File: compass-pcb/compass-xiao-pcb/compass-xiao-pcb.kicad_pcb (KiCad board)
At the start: 2 copper layers, 72.2 x 72 mm, 24 parts

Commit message: polishing
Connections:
- QMC5883L pad 3: (no net) -> GND
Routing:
- net (no net): track 1108.9 -> 1118.5 mm
- net GND: track 1.55 -> 8.21 mm
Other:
- board text removed: "VCC GND SCL SDA"

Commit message: fixing ground
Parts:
- REF**: value TX, RX, GND -> TX, RX
- REF**: value SCL,SDA,VCC -> VCC,SCL,SDA
- moved REF** 5.20 mm to (241.2, 47.3), turned to 90 degrees
- moved REF** 5.19 mm to (241.2, 51.6), turned to 90 degrees
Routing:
- net (no net): track 1118.5 -> 1129.4 mm
- net GND: track 8.21 -> 16.7 mm, vias 0 -> 1

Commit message: lots of pcb fixes
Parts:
- moved 49E Hall 168.5 mm to (74.5, 92.7)
- moved A1SHB 168.4 mm to (40.2, 84.6)
- moved QMC5883L 168.4 mm to (28.4, 78.7)
- moved USB / Charge 168.4 mm to (45.9, 65.4)
- moved 10K 168.4 mm to (35.0, 37.4)
- moved 10K 168.4 mm to (40.3, 80.9)
- moved 1N4148 168.4 mm to (39.1, 35.3)
- moved 51 168.4 mm to (40.2, 93.1)
- moved 51 168.4 mm to (40.3, 88.4)
- moved 51 168.4 mm to (40.2, 90.7)
- moved A1SHB 168.4 mm to (40.2, 31.3)
- moved Battery 168.4 mm to (71.4, 88.9)
- moved LEDs 168.4 mm to (30.0, 84.0)
- moved REF** 168.4 mm to (73.7, 27.2)
- moved REF** 168.4 mm to (26.0, 58.3)
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- renumbered 56 to 51
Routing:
- net GND: track 16.7 -> 23.1 mm
- net (no net): track 1129.4 -> 1134.9 mm
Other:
- outline, holes or cut-outs redrawn
- board text added: "3.7V 5V D- D+ GND"
- board text removed: "3.7V 5V D+ D- GND"

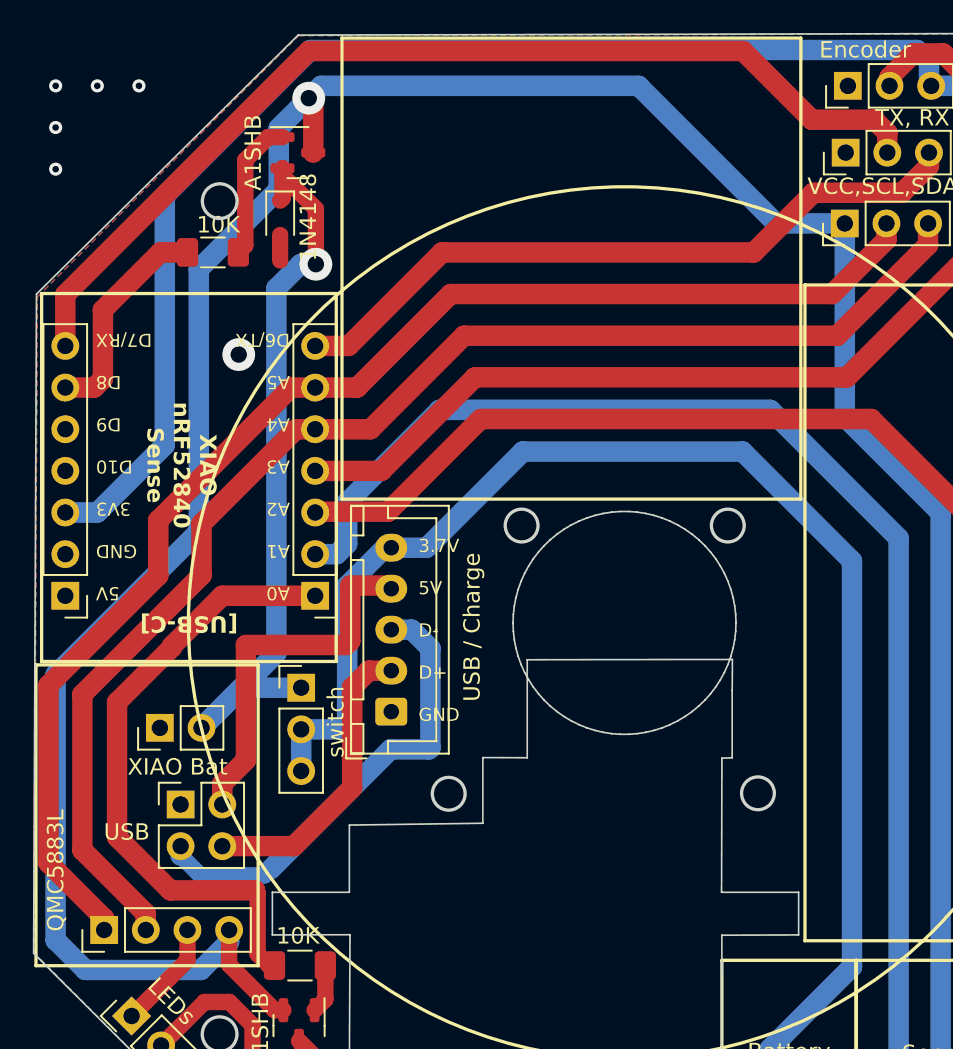
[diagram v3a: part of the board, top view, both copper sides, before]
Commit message: optimizing for cricut
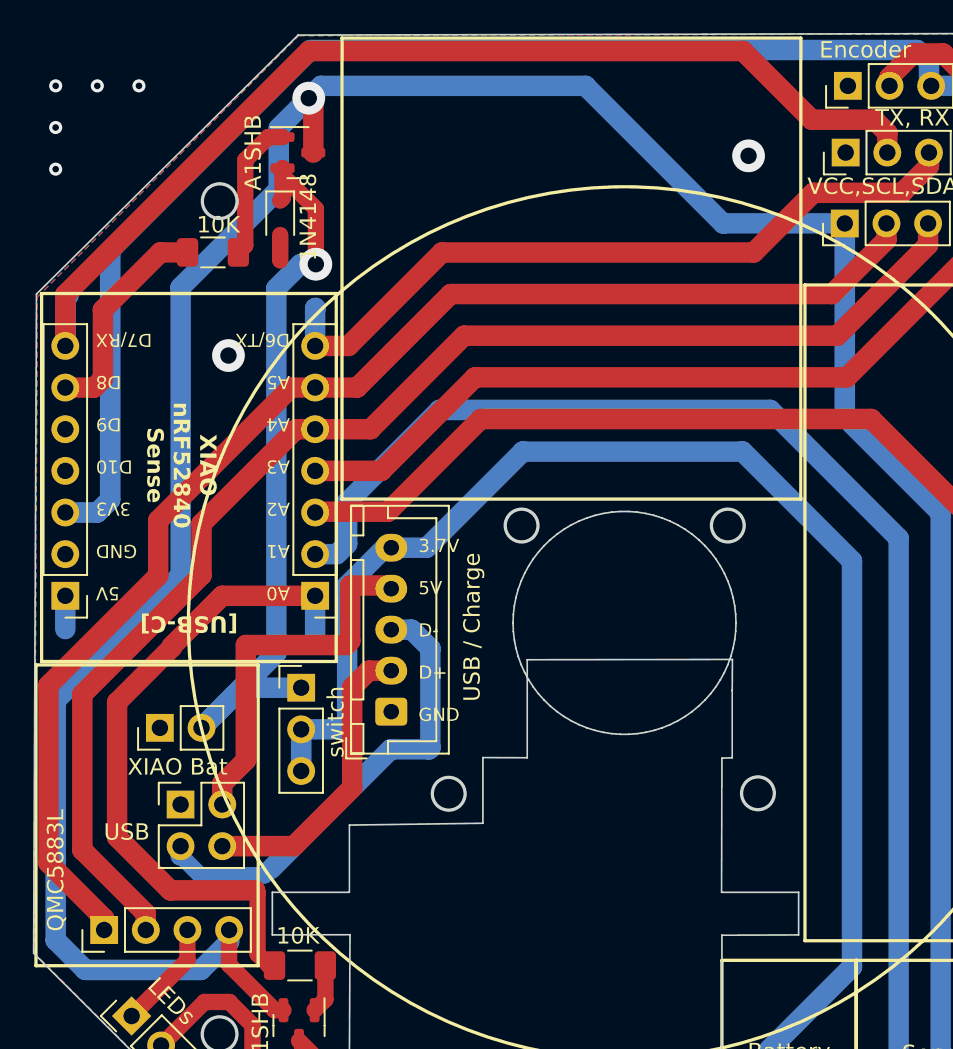
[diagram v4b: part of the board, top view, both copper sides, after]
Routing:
- net (no net): track 1134.9 -> 1145.3 mm
- net GND: vias 1 -> 2

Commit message: more polishing
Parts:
- moved 49E Hall 0.17 mm to (74.5, 92.5)
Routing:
- net (no net): track 1145.3 -> 1155.2 mm
- net GND: track 23.1 -> 31.4 mm

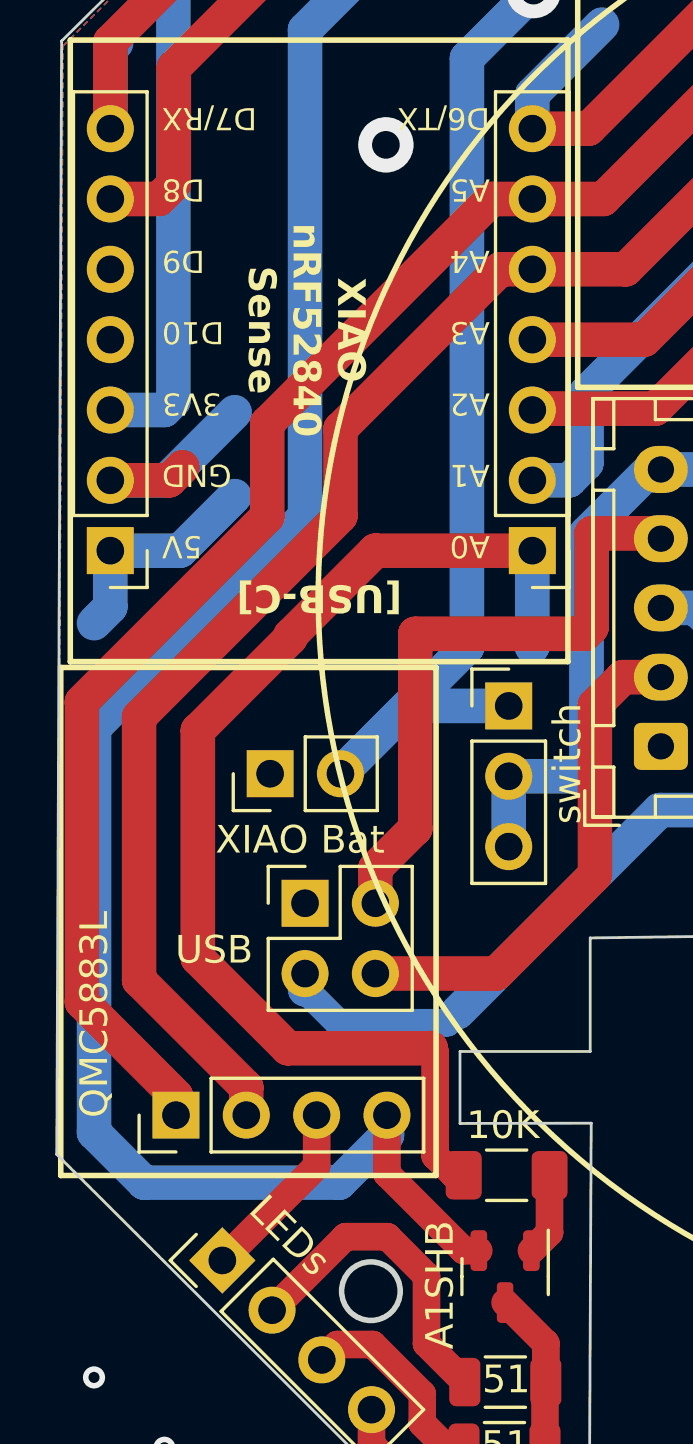
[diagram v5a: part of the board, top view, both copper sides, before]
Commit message: fixing SCL/SDA connection to compass
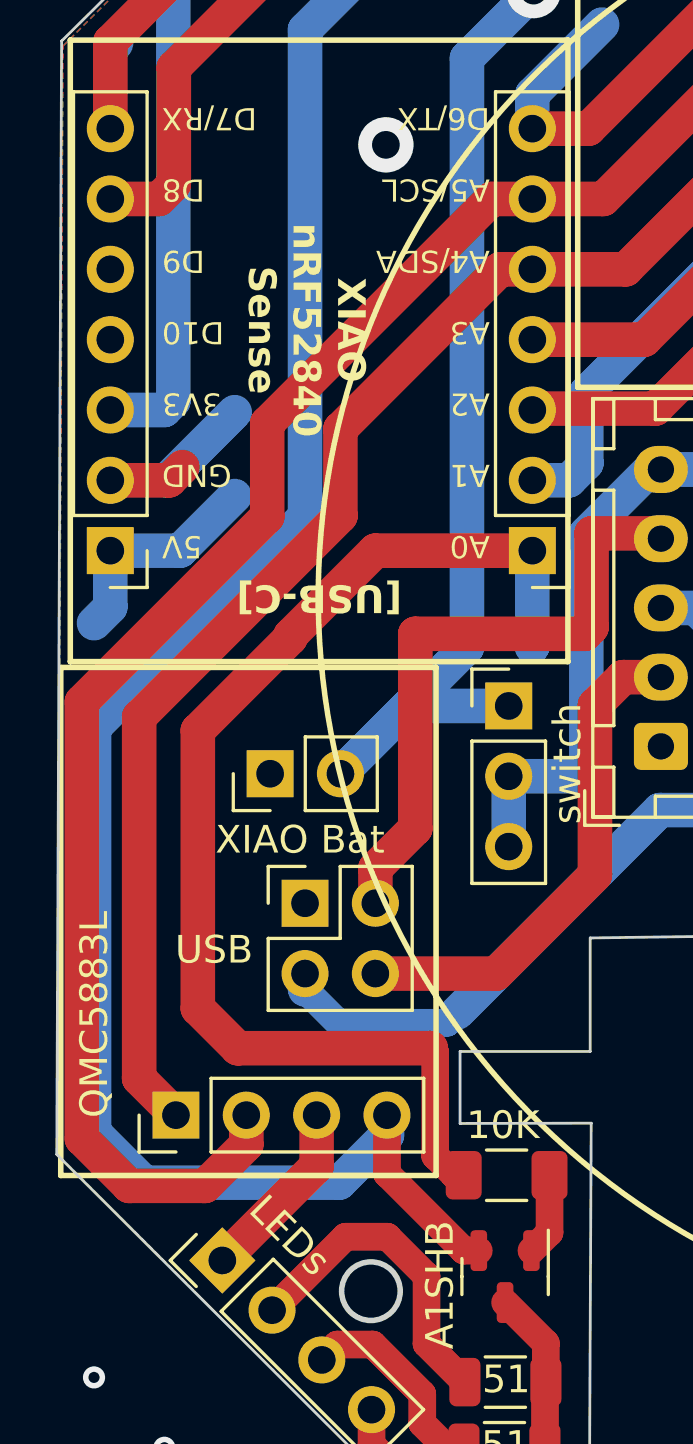
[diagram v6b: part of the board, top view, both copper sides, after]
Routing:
- net (no net): track 1155.2 -> 1163.0 mm
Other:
- board text added: "A0 A1 A2 A3 A4/SDA A5/SCL D6/TX"
- board text removed: "A0 A1 A2 A3 A4 A5 D6/TX"

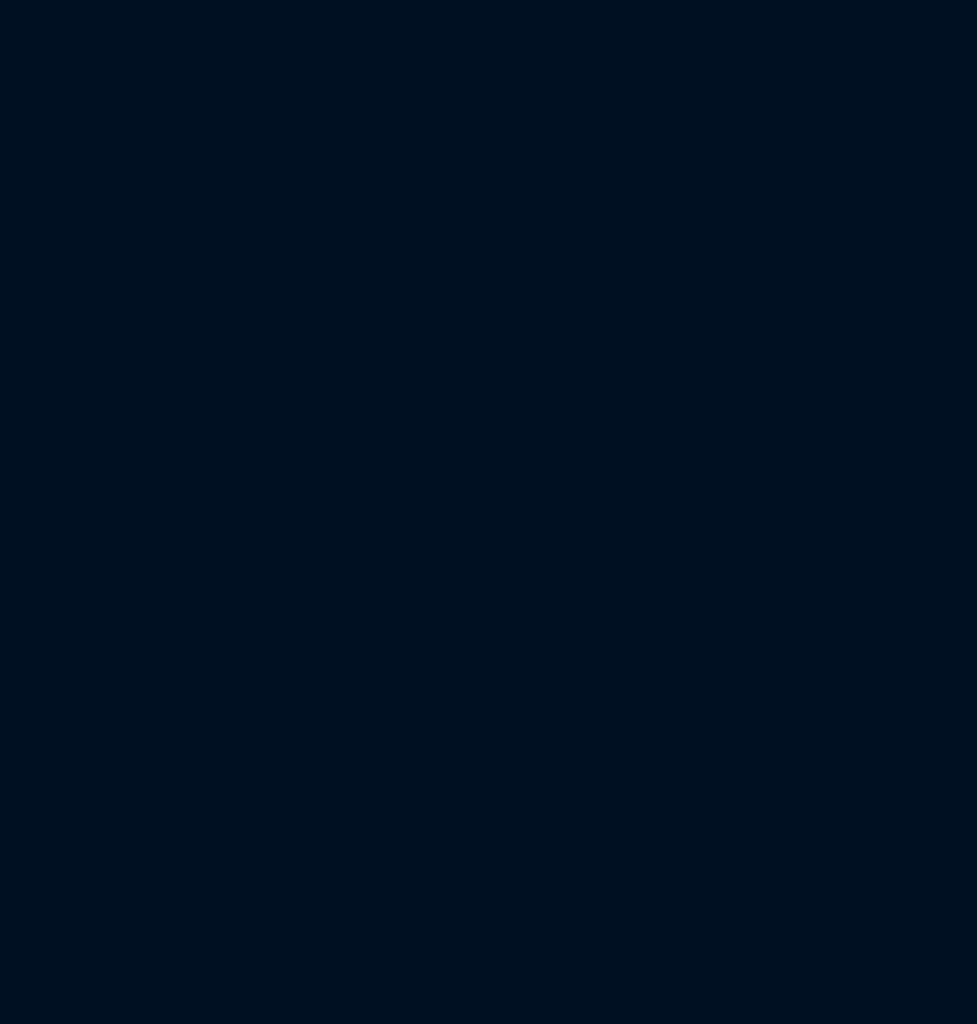
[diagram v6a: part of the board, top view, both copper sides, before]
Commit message: New model with n-channel mosfet for improved power management
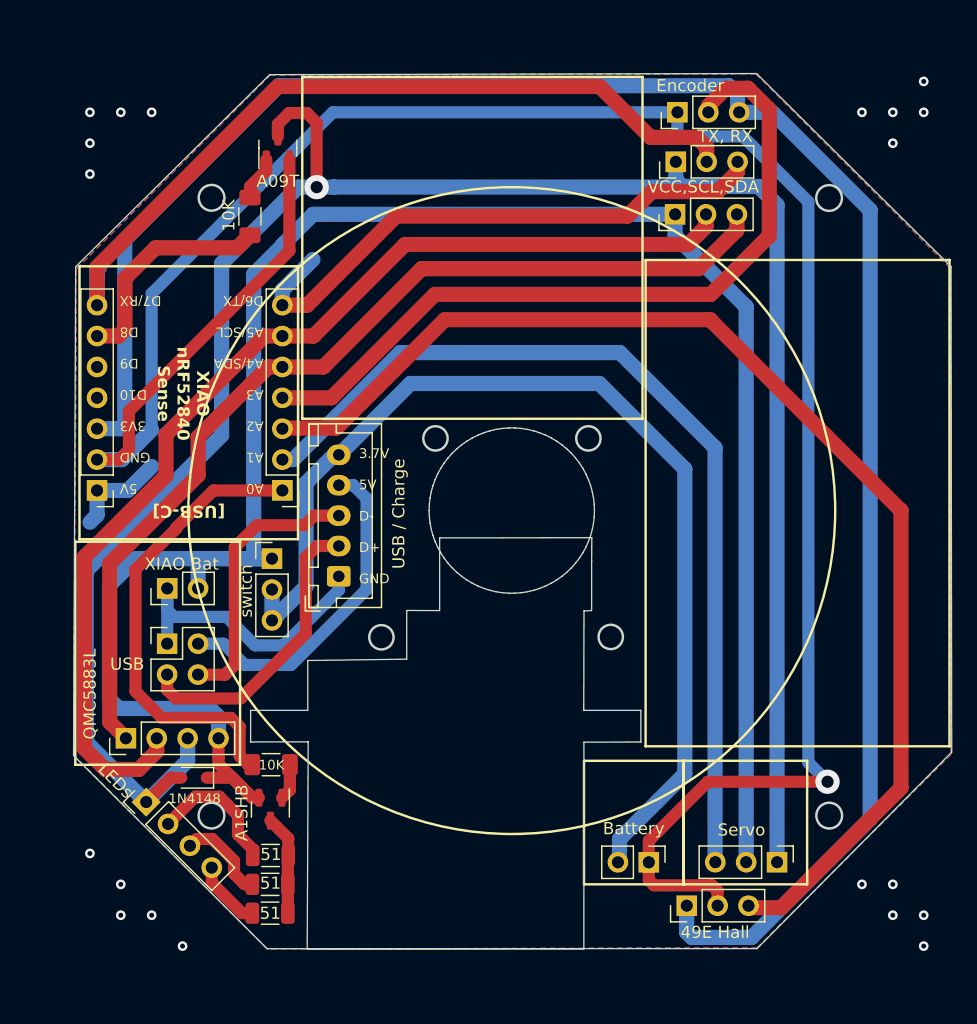
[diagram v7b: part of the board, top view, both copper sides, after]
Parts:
- added 10K: R1002, Resistor_SMD:R_1206_3216Metric_Pad1.30x1.75mm_HandSolder, F.Cu at (136.1, 112.3)
- added 10K: R1002, Resistor_SMD:R_1206_3216Metric_Pad1.30x1.75mm_HandSolder, F.Cu at (134.4, 67.2)
- added 1N4148: D_SOD-323, Diode_SMD:D_SOD-323, F.Cu at (129.8, 113.4)
- added 49E Hall: PinHeader_1x03_P2.54mm_Vertical, Connector_PinHeader_2.54mm:PinHeader_1x03_P2.54mm_Vertical, F.Cu at (170.3, 123.9)
- added 51: R_1206_3216Metric, Resistor_SMD:R_1206_3216Metric, F.Cu at (136.1, 122.2)
- added 51: R_1206_3216Metric, Resistor_SMD:R_1206_3216Metric, F.Cu at (136.1, 119.8)
- added 51: R_1206_3216Metric, Resistor_SMD:R_1206_3216Metric, F.Cu at (136.1, 124.6)
- added A09T: SOT-23, Package_TO_SOT_SMD:SOT-23, F.Cu at (136.7, 61.6)
- added A1SHB: SOT-23, Package_TO_SOT_SMD:SOT-23, F.Cu at (136.1, 116.0)
- added Battery: PinHeader_1x02_P2.54mm_Vertical, Connector_PinHeader_2.54mm:PinHeader_1x02_P2.54mm_Vertical, F.Cu at (167.2, 120.4)
- added LEDs: PinHeader_1x04_P2.54mm_Vertical, Connector_PinHeader_2.54mm:PinHeader_1x04_P2.54mm_Vertical, F.Cu at (125.9, 115.4)
- added QMC5883L: PinHeader_1x04_P2.54mm_Vertical, Connector_PinHeader_2.54mm:PinHeader_1x04_P2.54mm_Vertical, F.Cu at (124.2, 110.2)
- added REF**: TX, RX, Connector_PinHeader_2.54mm:PinHeader_1x03_P2.54mm_Vertical, F.Cu at (169.4, 62.8)
- added REF**: Encoder, Connector_PinHeader_2.54mm:PinHeader_1x03_P2.54mm_Vertical, F.Cu at (169.6, 58.7)
- added REF**: PinHeader_1x07_P2.54mm_Vertical, Connector_PinHeader_2.54mm:PinHeader_1x07_P2.54mm_Vertical, F.Cu at (121.8, 89.8)
- added REF**: VCC,SCL,SDA, Connector_PinHeader_2.54mm:PinHeader_1x03_P2.54mm_Vertical, F.Cu at (169.4, 67.1)
- added REF**: PinHeader_1x07_P2.54mm_Vertical, Connector_PinHeader_2.54mm:PinHeader_1x07_P2.54mm_Vertical, F.Cu at (137.1, 89.8)
- added Servo: PinHeader_1x03_P2.54mm_Vertical, Connector_PinHeader_2.54mm:PinHeader_1x03_P2.54mm_Vertical, F.Cu at (177.8, 120.4)
- added USB / Charge: JST_XH_B5B-XH-A_1x05_P2.50mm_Vertical, Connector_JST:JST_XH_B5B-XH-A_1x05_P2.50mm_Vertical, F.Cu at (141.7, 96.9)
- added USB: PinHeader_2x02_P2.54mm_Vertical, Connector_PinHeader_2.54mm:PinHeader_2x02_P2.54mm_Vertical, F.Cu at (127.6, 102.4)
- added XIAO Bat: PinHeader_1x02_P2.54mm_Vertical, Connector_PinHeader_2.54mm:PinHeader_1x02_P2.54mm_Vertical, F.Cu at (127.6, 97.8)
- added switch: PinHeader_1x03_P2.54mm_Vertical, Connector_PinHeader_2.54mm:PinHeader_1x03_P2.54mm_Vertical, F.Cu at (136.2, 95.4)
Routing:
- net (no net): track 1163.0 -> 1942.2 mm, vias 22 -> 42
- net GND: track 31.4 -> 245.2 mm, vias 2 -> 3
- net 3.7V: track 0.00 -> 183.1 mm
- net NEG: track 0.00 -> 176.5 mm, vias 0 -> 1
- net 3.3V: track 0.00 -> 160.7 mm
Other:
- board size 72.2 x 72 mm -> 168.1 x 103.4 mm

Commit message: some pcb polishing
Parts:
- moved A09T 0.94 mm to (135.8, 61.9)
- moved 51 0.67 mm to (136.4, 119.2)
- moved 51 0.66 mm to (136.4, 121.6)
- moved 51 0.61 mm to (136.3, 124.0)
- moved 10K 0.44 mm to (134.0, 67.2)
- moved A1SHB 0.36 mm to (136.2, 115.7)
- moved 1N4148 0.22 mm to (129.7, 113.2)
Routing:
- net GND: track 245.2 -> 325.8 mm
- net 3.7V: track 183.1 -> 171.6 mm
- net (no net): track 1942.2 -> 1950.7 mm
- net NEG: track 176.5 -> 174.7 mm
